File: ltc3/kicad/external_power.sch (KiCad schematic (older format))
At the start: 40 parts, among them IC2 TLP3542, IC3 TLP3542, IC4 TLP3542, IC701 TLP3542, M1 W28-XQ1A-1, M2 W28-XQ1A-1, M3 W28-XQ1A-1, M4 W28-XQ1A-1, P3 CONN_EXT_PWR_3, P4 CONN_EXT_PWR_2, P5 CONN_EXT_PWR_4, P6 CONN_01X10, P7 CONN_01X08, P701 CONN_EXT_PWR_1, P8 CONN_01X10, P9 CONN_01X08, Q1 PMV45EN, Q2 PMV45EN, Q3 PMV45EN, Q701 PMV45EN, SW4 SP3T, SW5 SP3T, SW6 SP3T, SW7 SP3T

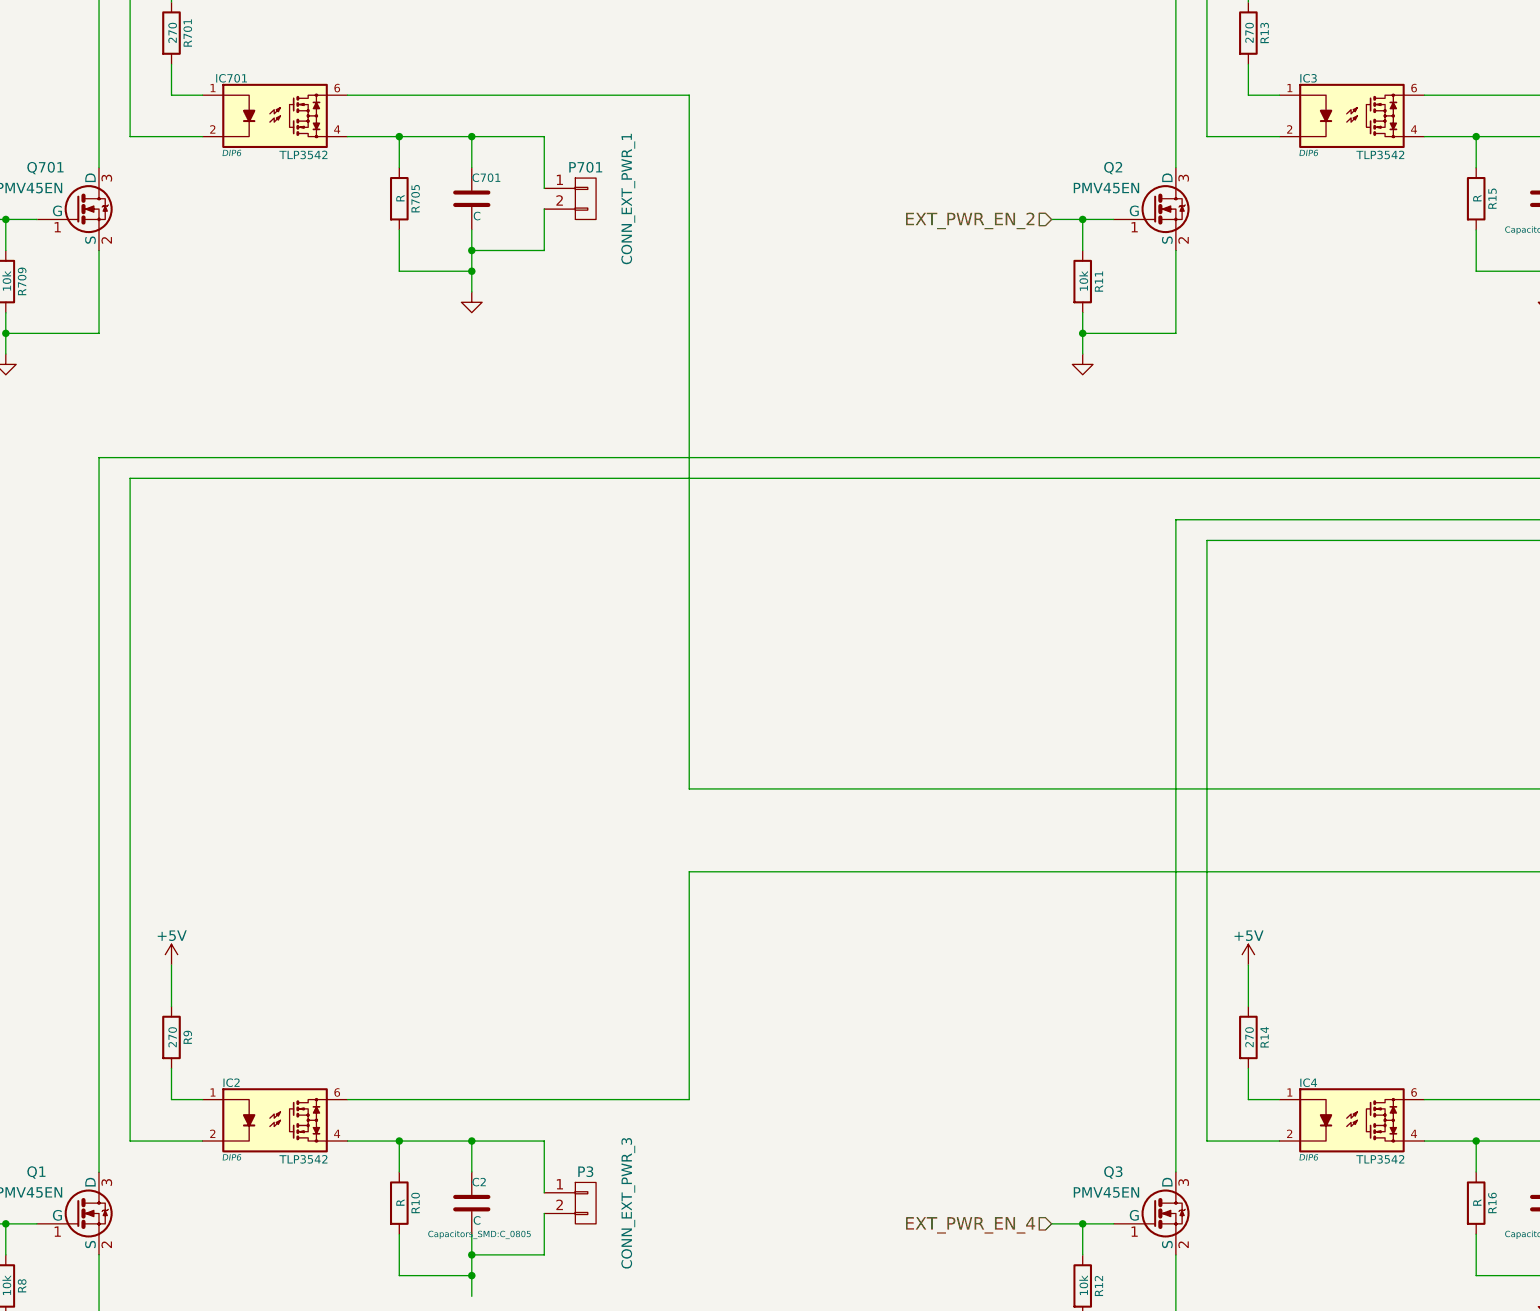
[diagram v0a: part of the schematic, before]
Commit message: Assigned more footprints, created PSOP-6 and PTN78020W.
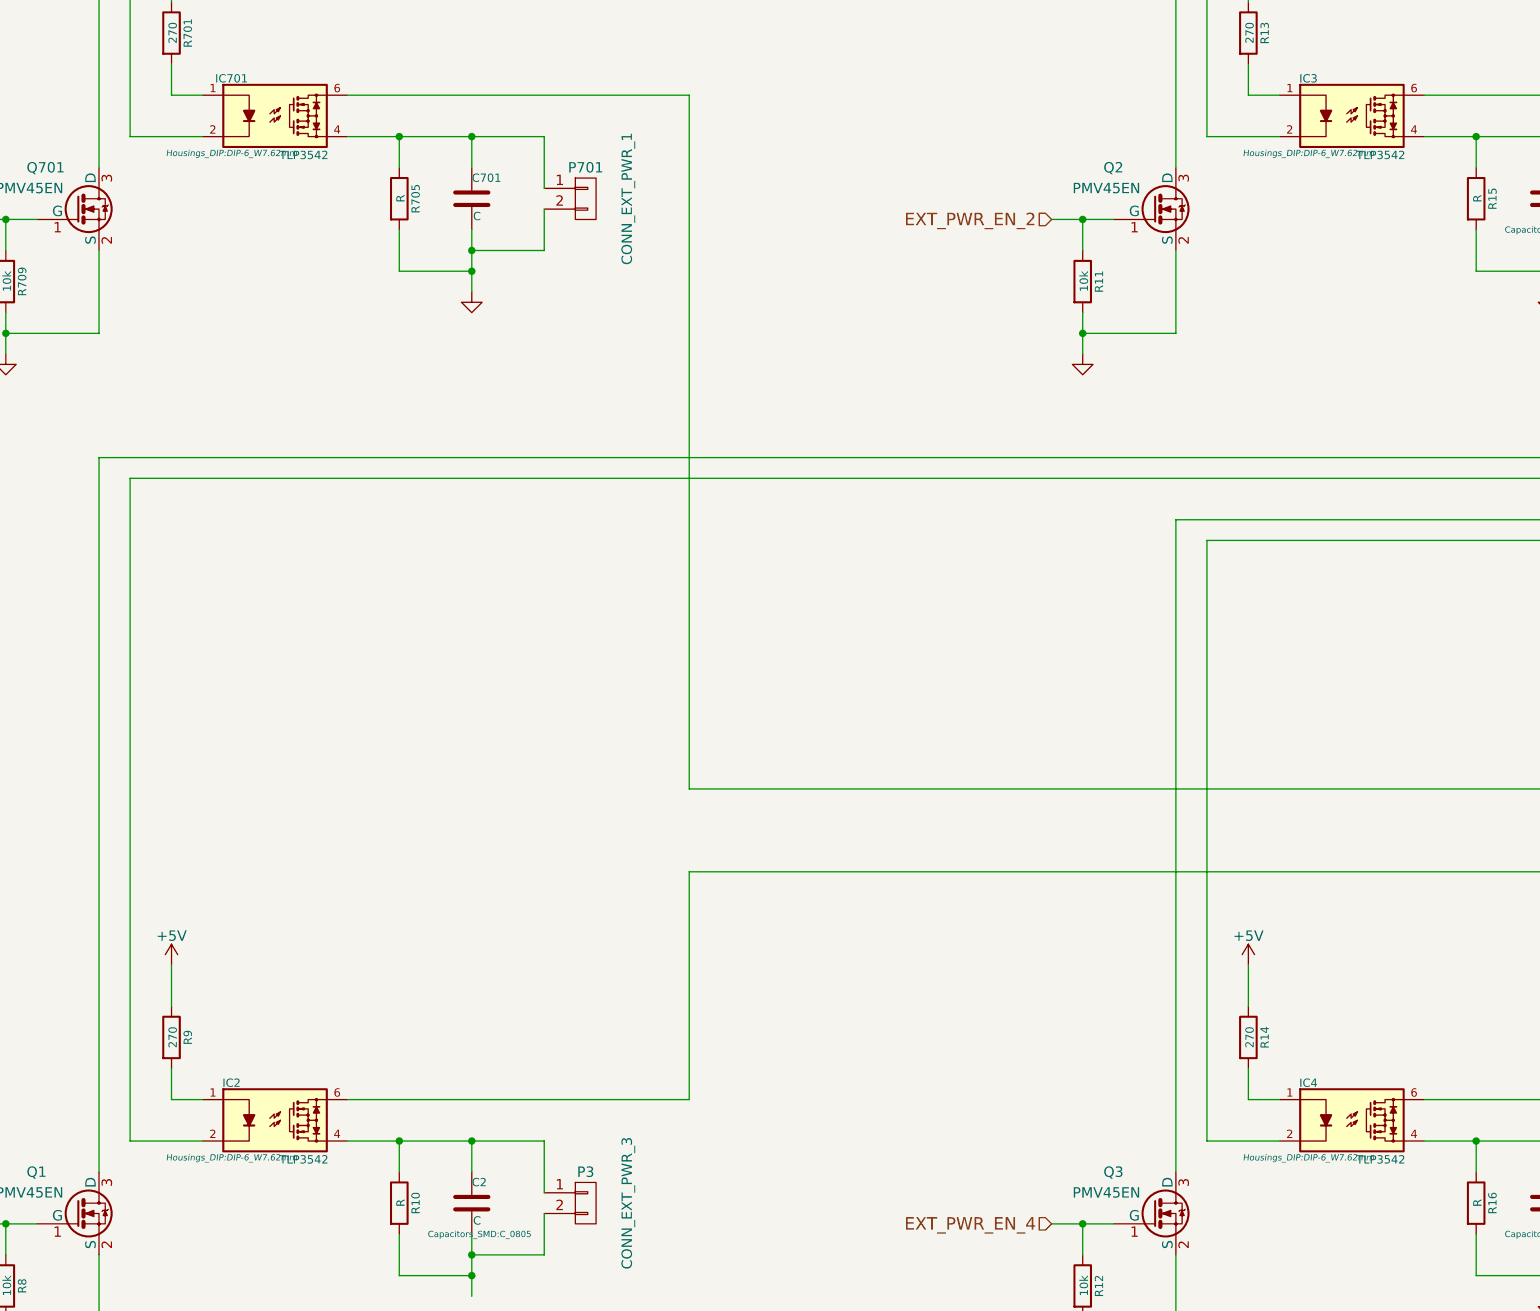
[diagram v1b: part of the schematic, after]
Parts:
- IC2, IC3, IC4, IC701: footprint DIP6 -> Housings_DIP:DIP-6_W7.62mm
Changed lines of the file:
@@
 LIBS:battery_single_cell
 LIBS:breakers
-LIBS:Launch_Tower_Computer_III-cache
 EELAYER 25 0
 EELAYER END
@@
 EXT_PWR_EN_1
 $Comp
-L GND #PWR0155
+L GND #PWR0160
 U 1 1 557E02AD
 P 1650 4100
-F 0 "#PWR0155" H 1650 4100 30  0001 C CNN
+F 0 "#PWR0160" H 1650 4100 30  0001 C CNN
 F 1 "GND" H 1650 4030 30  0001 C CNN
 F 2 "" H 1650 4100 60  0000 C CNN
@@
 $EndComp
 $Comp
-L GND #PWR0156
+L GND #PWR0161
 U 1 1 557E02DD
 P 3900 3800
-F 0 "#PWR0156" H 3900 3800 30  0001 C CNN
+F 0 "#PWR0161" H 3900 3800 30  0001 C CNN
 F 1 "GND" H 3900 3730 30  0001 C CNN
 F 2 "" H 3900 3800 60  0000 C CNN
@@
 F 0 "IC701" H 2740 3230 40  0000 C CNN
 F 1 "TLP3542" H 3090 2860 40  0000 C CNN
-F 2 "DIP6" H 2740 2870 30  0000 C CIN
+F 2 "Housings_DIP:DIP-6_W7.62mm" H 2740 2870 30  0000 C CIN
 F 3 "" H 2950 3050 60  0000 C CNN
 	1    2950 3000
@@
 $EndComp
 $Comp
-L +5V #PWR0157
+L +5V #PWR0162
 U 1 1 56544A2B
 P 2450 2200
-F 0 "#PWR0157" H 2450 2050 50  0001 C CNN
+F 0 "#PWR0162" H 2450 2050 50  0001 C CNN
 F 1 "+5V" H 2450 2340 50  0000 C CNN
 F 2 "" H 2450 2200 60  0000 C CNN
@@
 EXT_PWR_EN_2
 $Comp
-L GND #PWR0158
+L GND #PWR0163
 U 1 1 56CA75BB
 P 6850 4100
-F 0 "#PWR0158" H 6850 4100 30  0001 C CNN
+F 0 "#PWR0163" H 6850 4100 30  0001 C CNN
 F 1 "GND" H 6850 4030 30  0001 C CNN
 F 2 "" H 6850 4100 60  0000 C CNN
@@
 $EndComp
 $Comp
-L GND #PWR0159
+L GND #PWR0164
 U 1 1 56CA75CD
 P 9100 3800
-F 0 "#PWR0159" H 9100 3800 30  0001 C CNN
+F 0 "#PWR0164" H 9100 3800 30  0001 C CNN
 F 1 "GND" H 9100 3730 30  0001 C CNN
 F 2 "" H 9100 3800 60  0000 C CNN
@@
 F 0 "IC3" H 7940 3230 40  0000 C CNN
 F 1 "TLP3542" H 8290 2860 40  0000 C CNN
-F 2 "DIP6" H 7940 2870 30  0000 C CIN
+F 2 "Housings_DIP:DIP-6_W7.62mm" H 7940 2870 30  0000 C CIN
 F 3 "" H 8150 3050 60  0000 C CNN
 	1    8150 3000
@@
 $EndComp
 $Comp
-L +5V #PWR0160
+L +5V #PWR0165
 U 1 1 56CA760C
 P 7650 2200
-F 0 "#PWR0160" H 7650 2050 50  0001 C CNN
+F 0 "#PWR0165" H 7650 2050 50  0001 C CNN
 F 1 "+5V" H 7650 2340 50  0000 C CNN
 F 2 "" H 7650 2200 60  0000 C CNN
@@
 $EndComp
 $Comp
-L +12V #PWR0161
+L +12V #PWR0166
 U 1 1 56CA7612
 P 11800 5650
-F 0 "#PWR0161" H 11800 5500 50  0001 C CNN
+F 0 "#PWR0166" H 11800 5500 50  0001 C CNN
 F 1 "+12V" H 11800 5790 50  0000 C CNN
 F 2 "" H 11800 5650 60  0000 C CNN
@@
 EXT_PWR_EN_3
 $Comp
-L GND #PWR0162
+L GND #PWR0167
 U 1 1 56CA9336
 P 1650 8950
-F 0 "#PWR0162" H 1650 8950 30  0001 C CNN
+F 0 "#PWR0167" H 1650 8950 30  0001 C CNN
 F 1 "GND" H 1650 8880 30  0001 C CNN
 F 2 "" H 1650 8950 60  0000 C CNN
@@
 F 0 "IC2" H 2740 8080 40  0000 C CNN
 F 1 "TLP3542" H 3090 7710 40  0000 C CNN
-F 2 "DIP6" H 2740 7720 30  0000 C CIN
+F 2 "Housings_DIP:DIP-6_W7.62mm" H 2740 7720 30  0000 C CIN
 F 3 "" H 2950 7900 60  0000 C CNN
 	1    2950 7850
@@
 $EndComp
 $Comp
-L +5V #PWR0163
+L +5V #PWR0168
 U 1 1 56CA9387
 P 2450 7050
-F 0 "#PWR0163" H 2450 6900 50  0001 C CNN
+F 0 "#PWR0168" H 2450 6900 50  0001 C CNN
 F 1 "+5V" H 2450 7190 50  0000 C CNN
 F 2 "" H 2450 7050 60  0000 C CNN
@@
 EXT_PWR_EN_4
 $Comp
-L GND #PWR0164
+L GND #PWR0169
 U 1 1 56CA93AD
 P 6850 8950
-F 0 "#PWR0164" H 6850 8950 30  0001 C CNN
+F 0 "#PWR0169" H 6850 8950 30  0001 C CNN
 F 1 "GND" H 6850 8880 30  0001 C CNN
 F 2 "" H 6850 8950 60  0000 C CNN
@@
 $EndComp
 $Comp
-L GND #PWR0165
+L GND #PWR0170
 U 1 1 56CA93BF
 P 9100 8650
-F 0 "#PWR0165" H 9100 8650 30  0001 C CNN
+F 0 "#PWR0170" H 9100 8650 30  0001 C CNN
 F 1 "GND" H 9100 8580 30  0001 C CNN
 F 2 "" H 9100 8650 60  0000 C CNN
@@
 F 0 "IC4" H 7940 8080 40  0000 C CNN
 F 1 "TLP3542" H 8290 7710 40  0000 C CNN
-F 2 "DIP6" H 7940 7720 30  0000 C CIN
+F 2 "Housings_DIP:DIP-6_W7.62mm" H 7940 7720 30  0000 C CIN
 F 3 "" H 8150 7900 60  0000 C CNN
 	1    8150 7850
@@
 $EndComp
 $Comp
-L +5V #PWR0166
+L +5V #PWR0171
 U 1 1 56CA93FE
 P 7650 7050
-F 0 "#PWR0166" H 7650 6900 50  0001 C CNN
+F 0 "#PWR0171" H 7650 6900 50  0001 C CNN
 F 1 "+5V" H 7650 7190 50  0000 C CNN
 F 2 "" H 7650 7050 60  0000 C CNN
@@
 Manual Override Switches, Front Panel
 $Comp
-L GND #PWR0167
+L GND #PWR0172
 U 1 1 56DB5084
 P 11800 2800
-F 0 "#PWR0167" H 11800 2550 50  0001 C CNN
+F 0 "#PWR0172" H 11800 2550 50  0001 C CNN
 F 1 "GND" H 11808 2626 50  0001 C CNN
 F 2 "" H 11800 2800 50  0000 C CNN

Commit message: LTC3: Cosmetic changes; reference designator updates; etc.
1. Renamed "PHNTM*" reference designators to something more
   conventional and descriptive (e.g., "PHNTM*" to "BT*" for off-board
   batteries).
2. Cosmetic changes to battery management and BeagleBone schematics
   (normalizing text notes style, etc.).
3. Incremental progress on footprint assignment.
4. Imported netlist into PCB layout editor, just for grins.
   Everything fits into a 250x135mm board.  Only $260 for an OSH Park run!
   There may be some opportunities for improvement...
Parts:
- M1, M2, M3, M4, SW4, SW5, SW6, SW7: footprint (none) -> Oddities:Dummy_Empty
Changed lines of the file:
@@
 F 0 "M3" H 14750 7225 50  0000 C CNN
 F 1 "W28-XQ1A-1" H 14750 7025 50  0000 C CNN
-F 2 "" H 14750 7100 50  0001 C CNN
+F 2 "Oddities:Dummy_Empty" H 14750 7100 50  0001 C CNN
 F 3 "" H 14750 7100 50  0000 C CNN
 	1    14750 7100
@@
 F 0 "M4" H 15150 7225 50  0000 C CNN
 F 1 "W28-XQ1A-1" H 15150 7025 50  0000 C CNN
-F 2 "" H 15150 7100 50  0001 C CNN
+F 2 "Oddities:Dummy_Empty" H 15150 7100 50  0001 C CNN
 F 3 "" H 15150 7100 50  0000 C CNN
 	1    15150 7100
@@
 F 0 "M1" H 13950 7225 50  0000 C CNN
 F 1 "W28-XQ1A-1" H 13950 7025 50  0000 C CNN
-F 2 "" H 13950 7100 50  0001 C CNN
+F 2 "Oddities:Dummy_Empty" H 13950 7100 50  0001 C CNN
 F 3 "" H 13950 7100 50  0000 C CNN
 	1    13950 7100
@@
 F 0 "M2" H 14350 7225 50  0000 C CNN
 F 1 "W28-XQ1A-1" H 14350 7025 50  0000 C CNN
-F 2 "" H 14350 7100 50  0001 C CNN
+F 2 "Oddities:Dummy_Empty" H 14350 7100 50  0001 C CNN
 F 3 "" H 14350 7100 50  0000 C CNN
 	1    14350 7100
@@
 F 0 "SW4" V 13704 2648 50  0000 R CNN
 F 1 "SP3T" V 13796 2648 50  0000 R CNN
-F 2 "" H 13125 2975 50  0001 C CNN
+F 2 "Oddities:Dummy_Empty" H 13125 2975 50  0001 C CNN
 F 3 "" H 13125 2975 50  0000 C CNN
 	1    13750 2800
@@
 F 0 "SW5" V 14446 2648 50  0000 R CNN
 F 1 "SP3T" V 14354 2648 50  0000 R CNN
-F 2 "" H 13775 2975 50  0001 C CNN
+F 2 "Oddities:Dummy_Empty" H 13775 2975 50  0001 C CNN
 F 3 "" H 13775 2975 50  0000 C CNN
 	1    14400 2800
@@
 F 0 "SW6" V 15096 2648 50  0000 R CNN
 F 1 "SP3T" V 15004 2648 50  0000 R CNN
-F 2 "" H 14425 2975 50  0001 C CNN
+F 2 "Oddities:Dummy_Empty" H 14425 2975 50  0001 C CNN
 F 3 "" H 14425 2975 50  0000 C CNN
 	1    15050 2800
@@
 F 0 "SW7" V 15746 2648 50  0000 R CNN
 F 1 "SP3T" V 15654 2648 50  0000 R CNN
-F 2 "" H 15075 2975 50  0001 C CNN
+F 2 "Oddities:Dummy_Empty" H 15075 2975 50  0001 C CNN
 F 3 "" H 15075 2975 50  0000 C CNN
 	1    15700 2800

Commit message: Minor adjustment to BB cape footprint; more footprint assignments.
NB: "Valve" footprints are placeholder for components not yet
assigned.
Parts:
- P3, P4, P5, P701: footprint Pin_Headers:Pin_Header_Straight_1x02 -> Valves:VALVE-OCTAL
- P6: footprint Pin_Headers:Pin_Header_Straight_1x10 -> Connectors_Molex:Molex_Microfit3_Header_02x05_Angled_43045-100x
- P7: footprint Pin_Headers:Pin_Header_Straight_1x08 -> Connectors_Molex:Molex_Microfit3_Header_02x04_Angled_43045-080x
- P8: footprint Pin_Headers:Pin_Header_Straight_1x10 -> Oddities:Dummy_Empty
- P9: footprint Pin_Headers:Pin_Header_Straight_1x08 -> Oddities:Dummy_Empty
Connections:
- wire segments 172 -> 204
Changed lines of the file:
@@
 F 0 "P701" H 4450 3500 50  0000 C CNN
 F 1 "CONN_EXT_PWR_1" V 4650 3350 50  0000 C CNN
-F 2 "Pin_Headers:Pin_Header_Straight_1x02" H 4450 3350 60  0001 C CNN
+F 2 "Valves:VALVE-OCTAL" H 4450 3350 60  0001 C CNN
 F 3 "" H 4450 3350 60  0000 C CNN
 	1    4450 3350
@@
 F 0 "P4" H 9650 3500 50  0000 C CNN
 F 1 "CONN_EXT_PWR_2" V 9850 3350 50  0000 C CNN
-F 2 "Pin_Headers:Pin_Header_Straight_1x02" H 9650 3350 60  0001 C CNN
+F 2 "Valves:VALVE-OCTAL" H 9650 3350 60  0001 C CNN
 F 3 "" H 9650 3350 60  0000 C CNN
 	1    9650 3350
@@
 F 0 "P3" H 4450 8350 50  0000 C CNN
 F 1 "CONN_EXT_PWR_3" V 4650 8200 50  0000 C CNN
-F 2 "Pin_Headers:Pin_Header_Straight_1x02" H 4450 8200 60  0001 C CNN
+F 2 "Valves:VALVE-OCTAL" H 4450 8200 60  0001 C CNN
 F 3 "" H 4450 8200 60  0000 C CNN
 	1    4450 8200
@@
 F 0 "P5" H 9650 8350 50  0000 C CNN
 F 1 "CONN_EXT_PWR_4" V 9850 8200 50  0000 C CNN
-F 2 "Pin_Headers:Pin_Header_Straight_1x02" H 9650 8200 60  0001 C CNN
+F 2 "Valves:VALVE-OCTAL" H 9650 8200 60  0001 C CNN
 F 3 "" H 9650 8200 60  0000 C CNN
 	1    9650 8200
@@
 F 0 "P7" H 12250 6950 50  0000 L CNN
 F 1 "CONN_01X08" V 12400 6250 50  0000 L CNN
-F 2 "Pin_Headers:Pin_Header_Straight_1x08" H 12250 6450 50  0001 C CNN
+F 2 "Connectors_Molex:Molex_Microfit3_Header_02x04_Angled_43045-080x" H 12250 6450 50  0001 C CNN
 F 3 "" H 12250 6450 50  0000 C CNN
 	1    12250 6450
@@
 F 0 "P9" H 13000 6950 50  0000 L CNN
 F 1 "CONN_01X08" V 13150 6250 50  0000 L CNN
-F 2 "Pin_Headers:Pin_Header_Straight_1x08" H 13000 6450 50  0001 C CNN
+F 2 "Oddities:Dummy_Empty" H 13000 6450 50  0001 C CNN
 F 3 "" H 13000 6450 50  0000 C CNN
 	1    13000 6450
@@
 F 0 "P6" H 12250 2650 50  0000 L CNN
 F 1 "CONN_01X10" V 12400 1600 50  0000 L CNN
-F 2 "Pin_Headers:Pin_Header_Straight_1x10" H 12250 2100 50  0001 C CNN
+F 2 "Connectors_Molex:Molex_Microfit3_Header_02x05_Angled_43045-100x" H 12250 2100 50  0001 C CNN
 F 3 "" H 12250 2100 50  0000 C CNN
 	1    12250 2100
@@
 F 0 "P8" H 13000 2650 50  0000 L CNN
 F 1 "CONN_01X10" V 13150 1600 50  0000 L CNN
-F 2 "Pin_Headers:Pin_Header_Straight_1x10" H 13000 2100 50  0001 C CNN
+F 2 "Oddities:Dummy_Empty" H 13000 2100 50  0001 C CNN
 F 3 "" H 13000 2100 50  0000 C CNN
 	1    13000 2100
@@
 	2100 4000 2100 3600
 Wire Wire Line
-	1650 3900 1650 4100
+	1650 3900 1650 4000
+Wire Wire Line
+	1650 4000 1650 4100
 Wire Wire Line
 	3900 3050 3900 3200
@@
 	3550 3700 3550 3500
 Wire Wire Line
-	3900 3500 3900 3800
+	3900 3500 3900 3600
+Wire Wire Line
+	3900 3600 3900 3700
+Wire Wire Line
+	3900 3700 3900 3800
 Connection ~ 3900 3050
 Connection ~ 3550 3050
@@
 	3550 3050 3550 3200
 Wire Wire Line
-	3300 3050 4250 3050
+	3300 3050 3550 3050
+Wire Wire Line
+	3550 3050 3900 3050
+Wire Wire Line
+	3900 3050 4250 3050
 Wire Wire Line
 	2250 3050 2600 3050
@@
 	2450 2200 2450 2400
 Wire Wire Line
-	1500 3450 1800 3450
+	1500 3450 1650 3450
+Wire Wire Line
+	1650 3450 1800 3450
 Connection ~ 1650 3450
 Wire Wire Line
@@
 	7300 4000 7300 3600
 Wire Wire Line
-	6850 3900 6850 4100
+	6850 3900 6850 4000
+Wire Wire Line
+	6850 4000 6850 4100
 Wire Wire Line
 	9100 3050 9100 3200
@@
 	8750 3700 8750 3500
 Wire Wire Line
-	9100 3500 9100 3800
+	9100 3500 9100 3600
+Wire Wire Line
+	9100 3600 9100 3700
+Wire Wire Line
+	9100 3700 9100 3800
 Connection ~ 9100 3050
 Connection ~ 8750 3050
@@
 	8750 3050 8750 3200
 Wire Wire Line
-	8500 3050 9450 3050
+	8500 3050 8750 3050
+Wire Wire Line
+	8750 3050 9100 3050
+Wire Wire Line
+	9100 3050 9450 3050
 Wire Wire Line
 	7450 3050 7800 3050
@@
 	6850 3600 6850 3450
 Wire Wire Line
-	11800 5650 11800 6700
+	11800 5650 11800 6100
+Wire Wire Line
+	11800 6100 11800 6300
+Wire Wire Line
+	11800 6300 11800 6500
+Wire Wire Line
+	11800 6500 11800 6700
 Wire Wire Line
 	7650 2200 7650 2400
 Wire Wire Line
-	6700 3450 7000 3450
+	6700 3450 6850 3450
+Wire Wire Line
+	6850 3450 7000 3450
 Connection ~ 6850 3450
 Wire Wire Line
@@
 	2100 8850 2100 8450
 Wire Wire Line
-	1650 8750 1650 8950
+	1650 8750 1650 8850
+Wire Wire Line
+	1650 8850 1650 8950
 Wire Wire Line
 	3900 7900 3900 8050
@@
 	3550 8550 3550 8350
 Wire Wire Line
-	3900 8350 3900 8650
+	3900 8350 3900 8450
+Wire Wire Line
+	3900 8450 3900 8550
+Wire Wire Line
+	3900 8550 3900 8650
 Wire Wire Line
 	2100 4600 2100 8050
@@
 	3550 7900 3550 8050
 Wire Wire Line
-	3300 7900 4250 7900
+	3300 7900 3550 7900
+Wire Wire Line
+	3550 7900 3900 7900
+Wire Wire Line
+	3900 7900 4250 7900
 Wire Wire Line
 	2450 7700 2600 7700
@@
 	2450 7050 2450 7250
 Wire Wire Line
-	1500 8300 1800 8300
+	1500 8300 1650 8300
+Wire Wire Line
+	1650 8300 1800 8300
 Connection ~ 1650 8300
 Wire Wire Line
@@
 	7300 8850 7300 8450
 Wire Wire Line
-	6850 8750 6850 8950
+	6850 8750 6850 8850
+Wire Wire Line
+	6850 8850 6850 8950
 Wire Wire Line
 	9100 7900 9100 8050
@@
 	8750 8550 8750 8350
 Wire Wire Line
-	9100 8350 9100 8650
+	9100 8350 9100 8450
+Wire Wire Line
+	9100 8450 9100 8550
+Wire Wire Line
+	9100 8550 9100 8650
 Wire Wire Line
 	7300 4900 7300 8050
@@
 	8750 7900 8750 8050
 Wire Wire Line
-	8500 7900 9450 7900
+	8500 7900 8750 7900
+Wire Wire Line
+	8750 7900 9100 7900
+Wire Wire Line
+	9100 7900 9450 7900
 Wire Wire Line
 	7650 7700 7800 7700
@@
 	7650 7050 7650 7250
 Wire Wire Line
-	6700 8300 7000 8300
+	6700 8300 6850 8300
+Wire Wire Line
+	6850 8300 7000 8300
 Connection ~ 6850 8300
 Wire Wire Line
@@
 	12700 3750 12700 1400
 Wire Wire Line
-	11800 2450 11800 2800
+	11800 2450 11800 2550
+Wire Wire Line
+	11800 2550 11800 2800
 Wire Wire Line
 	11800 2550 12050 2550
@@
 	2100 4600 11300 4600
 Wire Wire Line
-	11300 4600 11300 2250
-Wire Wire Line
-	11500 4900 11500 2450
+	11300 4600 11300 2050
+Wire Wire Line
+	11500 4900 11500 2250
 Connection ~ 11800 2550
 Wire Wire Line
@@
 	13850 3100 13850 3400
 Wire Wire Line
-	13350 3400 15800 3400
-Wire Wire Line
-	13350 2450 13350 3400
+	13350 3400 13850 3400
+Wire Wire Line
+	13850 3400 14500 3400
+Wire Wire Line
+	14500 3400 15150 3400
+Wire Wire Line
+	15150 3400 15800 3400
+Wire Wire Line
+	13350 2450 13350 2550
+Wire Wire Line
+	13350 2550 13350 3400
 Wire Wire Line
 	13350 2550 13200 2550
@@
 	11300 2050 12050 2050
 Wire Wire Line
-	11600 5000 11600 2550
+	11600 5000 11600 2350
 Wire Wire Line
 	12050 2150 11400 2150
 Wire Wire Line
-	11400 2350 11400 4700
+	11400 2150 11400 4700
 Wire Wire Line
 	11600 2350 12050 2350

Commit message: LTC3: Progress on component value validation, footprint assignment.
1. Added datasheets for large-valued capacitors (Panasonic),
   high-current connectors (Molex MicroFit), etc.
2. Added footprint for BeagleBone Black cape connector.
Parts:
- renumbered C3 to C702, C2 to C703, C4 to C704, IC3 to IC702, IC2 to IC703, IC4 to IC704, M1 to M701, M2 to M702, M3 to M703, M4 to M704, P6 to P701, P8 to P702, P701 to P703, P4 to P704, P7 to P705, P9 to P706, P3 to P707, P5 to P708, Q2 to Q702, Q1 to Q703, Q3 to Q704, R13 to R702, R705 to R703, R15 to R704, R709 to R705, R11 to R706, R9 to R707, R14 to R708, R10 to R709, R16 to R710, R8 to R711, R12 to R712, SW4 to SW701, SW5 to SW702, SW6 to SW703, SW7 to SW704
